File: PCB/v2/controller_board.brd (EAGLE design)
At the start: 150 x 66 mm, 58 parts, among them M1 B4B-PH-K-S(LF)(SN), M1_TMC TMC2209_SILENTSTEPSTICK, M2 B4B-PH-K-S(LF)(SN), M2_TMC TMC2209_SILENTSTEPSTICK, M3 B4B-PH-K-S(LF)(SN), M3_TMC TMC2209_SILENTSTEPSTICK, M4 B4B-PH-K-S(LF)(SN), M4_TMC TMC2209_SILENTSTEPSTICK

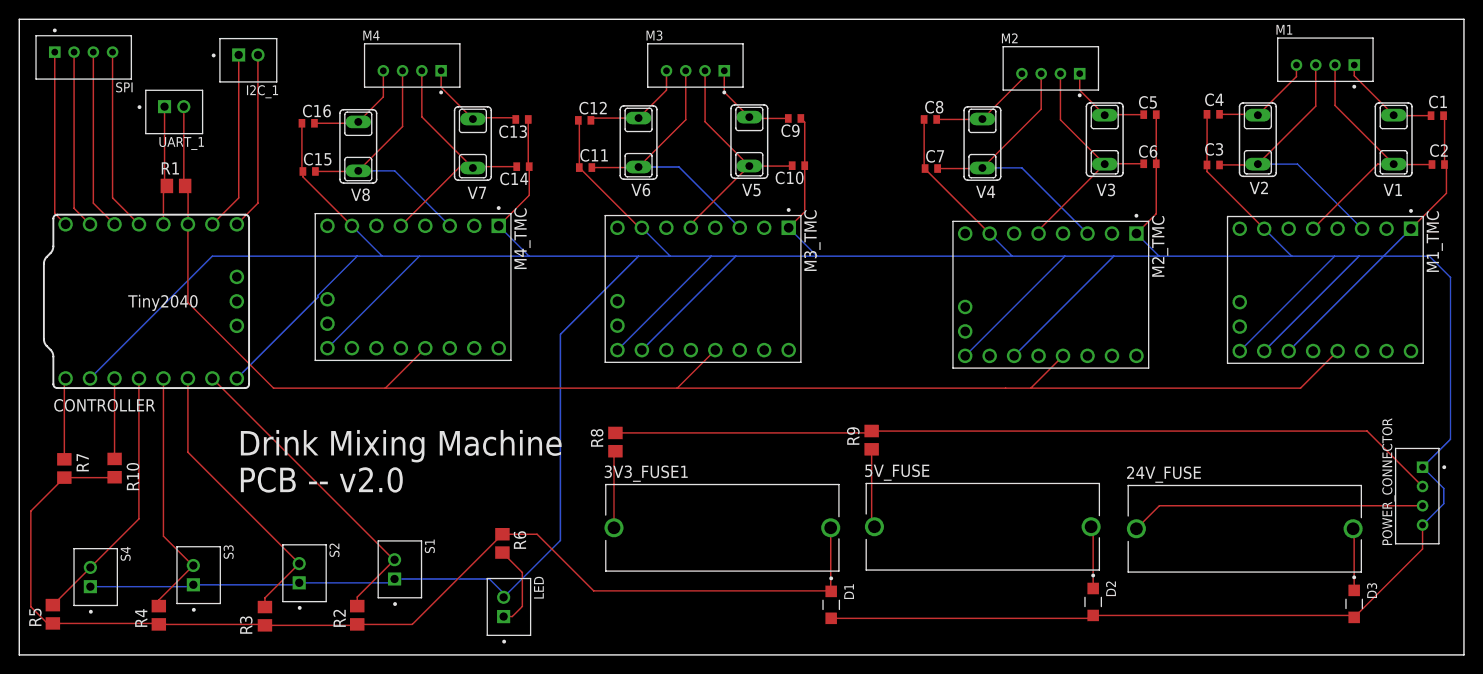
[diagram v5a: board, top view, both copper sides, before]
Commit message: feat(pcb): replace ESD protection with TVS-Diode
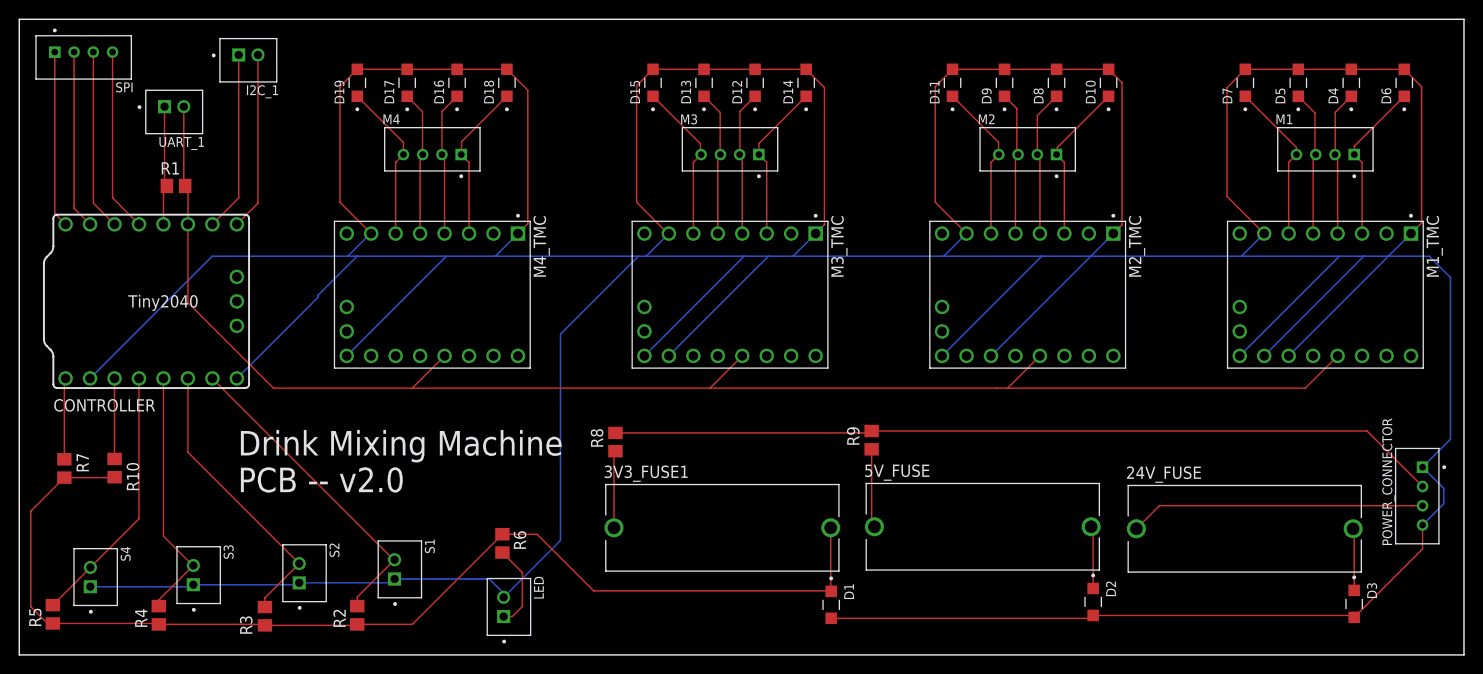
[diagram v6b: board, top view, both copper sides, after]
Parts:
- removed C1, C10, C11, C12, C13, C14, C15, C16, C2, C3, C4, C5, C6, C7, C8, C9: 470pF 100V, rcl:C0402
- removed V1, V2, V3, V4, V5, V6, V7, V8: S2220, varistor:S2220
- added D10, D11, D12, D13, D14, D15, D16, D17, D18, D19, D4, D5, D6, D7, D8, D9: PTVS24VS1UR, PTVS24VS1UR:TVS_PTVS24VS1UR
- moved M3 9.41 mm to (73.8, 52.5)
- moved M1 9.30 mm to (135.6, 52.5)
- moved M4 8.95 mm to (42.9, 52.5)
- moved M2 8.74 mm to (104.7, 52.5)
- moved M3_TMC 2.86 mm to (73.8, 37.4)
- moved M2_TMC 2.40 mm to (104.7, 37.4)
- moved M4_TMC 2.15 mm to (42.9, 37.4)
- moved M1_TMC 0.50 mm to (135.6, 37.4)
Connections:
- removed net N$22: C13.2, M4.1, M4_TMC.4, V7.2
- new net N$9: D12.C, M3.2, M3_TMC.4
- net GND: now also D10.A, D11.A, D12.A, D13.A, D14.A, D15.A, D16.A, D17.A, D18.A, D19.A, D4.A, D5.A, D6.A, D7.A, D8.A, D9.A; no longer C1.1, C10.1, C11.1, C12.1, C13.1, C14.1, C15.1, C16.1, C2.1, C3.1, C4.1, C5.1, C6.1, C7.1, C8.1, C9.1
- net N$10: now also D15.C; no longer C12.2, V6.1
- net N$11: now also D13.C, M3_TMC.5; no longer C11.2, M3_TMC.3, V6.2
- net N$12: now also D14.C, M3_TMC.3; no longer C9.2, M3_TMC.4, V5.2
- net N$13: now also D16.C, M4_TMC.4; no longer C14.2, M4_TMC.5, V7.1
- net N$14: now also D19.C, M4.4, M4_TMC.6; no longer C10.2, M3.2, M3_TMC.5, V5.1
- net N$15: now also D17.C, M4.3, M4_TMC.5; no longer C16.2, M4.4, M4_TMC.6, V8.1
- net N$16: now also D18.C, M4.1; no longer C15.2, M4.3, V8.2
- net N$19: now also D7.C, M1.4, M1_TMC.6; no longer C3.2, M1.3, M1_TMC.3, V2.2
- net N$2: now also D4.C, M1_TMC.4; no longer C2.2, M1_TMC.5, V1.1
- net N$26: now also D5.C, M1.3, M1_TMC.5; no longer C1.2, M1.1, M1_TMC.4, V1.2
- net N$4: now also D6.C, M1.1, M1_TMC.3; no longer C4.2, M1.4, M1_TMC.6, V2.1
- net N$5: now also D8.C, M2_TMC.4; no longer C6.2, M2_TMC.5, V3.1
- net N$6: now also D11.C; no longer C8.2, V4.1
- net N$7: now also D9.C, M2_TMC.5; no longer C7.2, M2_TMC.3, V4.2
- net N$8: now also D10.C, M2_TMC.3; no longer C5.2, M2_TMC.4, V3.2
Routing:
- net GND: track 597.6 -> 704.1 mm
- net N$22: track 24.2 -> 0.00 mm
- net N$7: track 30.7 -> 15.0 mm
- net N$9: track 0.00 -> 15.0 mm
- net N$11: track 30.0 -> 15.1 mm
- net N$19: track 30.4 -> 16.8 mm
- net N$2: track 28.0 -> 15.1 mm
- net N$16: track 28.6 -> 16.6 mm
- net N$13: track 27.0 -> 15.0 mm
- net LOW_POWER: track 391.1 -> 379.8 mm
- net N$5: track 25.4 -> 15.2 mm
- net N$26: track 25.0 -> 15.2 mm
- net N$15: track 24.3 -> 15.0 mm
- net N$14: track 25.2 -> 16.6 mm
- net N$6: track 24.4 -> 16.6 mm
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
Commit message: feat(pcb): add TMC enable pin
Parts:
- removed I2C_1: B2B-PH-K-S(LF)(SN), B2B-PH-K-S_LF__SN_:JST_B2B-PH-K-S(LF)(SN)
- removed SPI: B4B-PH-K-S(LF)(SN), B4B-PH-K-S_LF__SN_:JST_B4B-PH-K-S(LF)(SN)
- added R11: 0R, rcl:R0805
- added SPI_I2C: B4B-PH-K-S(LF)(SN), B4B-PH-K-S_LF__SN_:JST_B4B-PH-K-S(LF)(SN)
- moved D2 27.2 mm to (84.3, 4.70), flipped to the bottom
- moved 5V_FUSE 27.1 mm to (72.9, 13.1)
- moved 3V3_FUSE1 27.1 mm to (100.1, 13.1)
- moved D1 27.0 mm to (111.3, 4.70), flipped to the bottom
- moved R8 26.9 mm to (88.8, 22.2), flipped to the bottom
- moved R9 26.9 mm to (61.6, 22.2), flipped to the bottom
- moved R3 7.65 mm to (24.1, 11.5), flipped to the bottom, turned to 90 degrees
- moved R4 7.47 mm to (13.7, 11.5), flipped to the bottom, turned to 90 degrees
- moved R2 7.43 mm to (34.9, 11.5), flipped to the bottom, turned to 90 degrees
- moved R5 7.33 mm to (3.22, 11.5), flipped to the bottom, turned to 90 degrees
- moved UART_1 5.28 mm to (20.7, 58.9)
- moved R1 4.28 mm to (20.4, 49.8)
- moved LED 3.55 mm to (51.8, 8.41), turned to 90 degrees
- moved R6 2.68 mm to (47.5, 11.5), flipped to the bottom
- moved R7 1.73 mm to (4.74, 21.1), flipped to the bottom
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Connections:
- removed net SCL: CONTROLLER.7, I2C_1.2
- removed net SDA: CONTROLLER.6, I2C_1.1
- new net 3V3: 3V3_FUSE1.2, D1.C, R11.2
- new net TMC_EN: CONTROLLER.7, M1_TMC.16, M2_TMC.16, M3_TMC.16, M4_TMC.16
- net CS: now also SPI_I2C.2; no longer SPI.2
- net GND: no longer M1_TMC.16, M2_TMC.16, M3_TMC.16, M4_TMC.16
- net LOW_POWER: now also R11.1; no longer 3V3_FUSE1.2, D1.C
- net RX: now also SPI_I2C.1; no longer SPI.1
- net SCK: now also SPI_I2C.3; no longer SPI.3
- net TX: now also SPI_I2C.4; no longer SPI.4
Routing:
- net GND: track 704.1 -> 133.4 mm, vias 0 -> 8
- net TMC_EN: track 0.00 -> 133.6 mm
- net LOW_POWER: track 379.8 -> 316.6 mm
- net 24V: track 154.5 -> 188.9 mm, vias 0 -> 1
- net 3V3: track 0.00 -> 19.6 mm
- net SDA: track 18.7 -> 0.00 mm
- net UART: track 159.2 -> 177.8 mm
- net SCL: track 18.5 -> 0.00 mm
- net N$20: track 12.5 -> 16.7 mm
- net SCK: track 18.8 -> 14.9 mm
- net TX: track 19.0 -> 15.1 mm
- net CS: track 18.6 -> 14.9 mm
- net N$17: track 8.83 -> 5.32 mm
- net RX: track 18.3 -> 15.1 mm
- net N$18: track 8.45 -> 6.70 mm
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- added copper zone on layer 15, net GND
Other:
- board text added: "Drink Mixing Machine PCB – v3.0"
- board text removed: "Drink Mixing Machine PCB -- v2.0"
